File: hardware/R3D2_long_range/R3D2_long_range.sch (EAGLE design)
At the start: 64 parts, among them IC1 ATXMEGA64DA-AU, IC2 NCV8774DT33RKG, IC3 MAX3232CSE, T1 MMBT2222LT1G, T2 ZXMP6A17E6TA, T3 DMN6068SE

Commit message: routing board and remarks taken into account in sch
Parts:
- added C19: 100nF 50V, robotter_capacitor:100NF-E
- added R23, R24: 270-E, robotter_resistor:270-E
- added R25: 10K-F, robotter_resistor:10K-F
- added R26: 150K-F, robotter_resistor:150K-F
- IC1: value ATXMEGA64DA-AU -> ATXMEGA64D4-AU
- PH1: value GP1S58VJ000F -> EESX1106; device robotter_ic:GP1S58VJ000F -> robotter_ic:EESX1106
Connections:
- removed net N$12: IC1.OC0D/PE3, R12.1
- new net LED_COM_3V3: IC1.PC0/OC0A/SDA, R12.1
- new net N$17: IR-SENSOR.2, R23.1
- new net N$18: IR-SENSOR.1, R24.1
- new net VBAT_0-2V: C19.1, IC1.PB2/ADCA10, R25.2, R26.1
- net +24V: now also R26.2
- net GND: now also C19.2, IC1.PB3/ADCA11, R25.1
- net LONG_RANGE_LED_3V3: now also IC1.PA3/ADCA3, R23.2; no longer IC1.PB0/ADCA8/AREF, IR-SENSOR.2
- net LONG_RANGE_SENSOR_OUTPUT_3V3: now also IC1.PC2/OC0C/RXD0; no longer IC1.PC1/OC0B/XCK0/SCL
- net MIRROR_INDEX_3V3: now also IC1.PC3/OC0D/TXD0, IC1.XCK0/OC0B/PD1; no longer IC1.PC5/OC1B/MOSI
- net MOTOR_PWM_3V3: now also IC1.SDA/OC0A/PE0; no longer IC1.OC0A/PD0
- net N$10: now also IC1.OC0D/PE3; no longer IC1.OC0C/PE2
- net N$9: now also IC1.OC0C/PE2; no longer IC1.SCL/OC0B/PE1
- net ON/OFF_SENSOR_3V3: now also IC1.SCL/OC0B/PE1
- net SHORT_RANGE_LED_3V3: now also IC1.PA4/ADCA4, R24.2; no longer IC1.PB1/ADCA9, IR-SENSOR.1
- net SHORT_RANGE_SENSOR_OUTPUT_3V3: now also IC1.PC1/OC0B/XCK0/SCL; no longer IC1.PC2/OC0C/RXD0
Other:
- note added: "BATTERY : 12-30V SUPPLY VOLTAGE"
- note added: "Resistor divider is calculated to output 2V when battery voltage is 31V"
- note added: "Use INTVCC as reference voltage of ADC"
- moved on the sheet: BAT-1, BAT-2, C11, C12, C13, COM, D4, ERROR, IC2, R10, R12, R9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

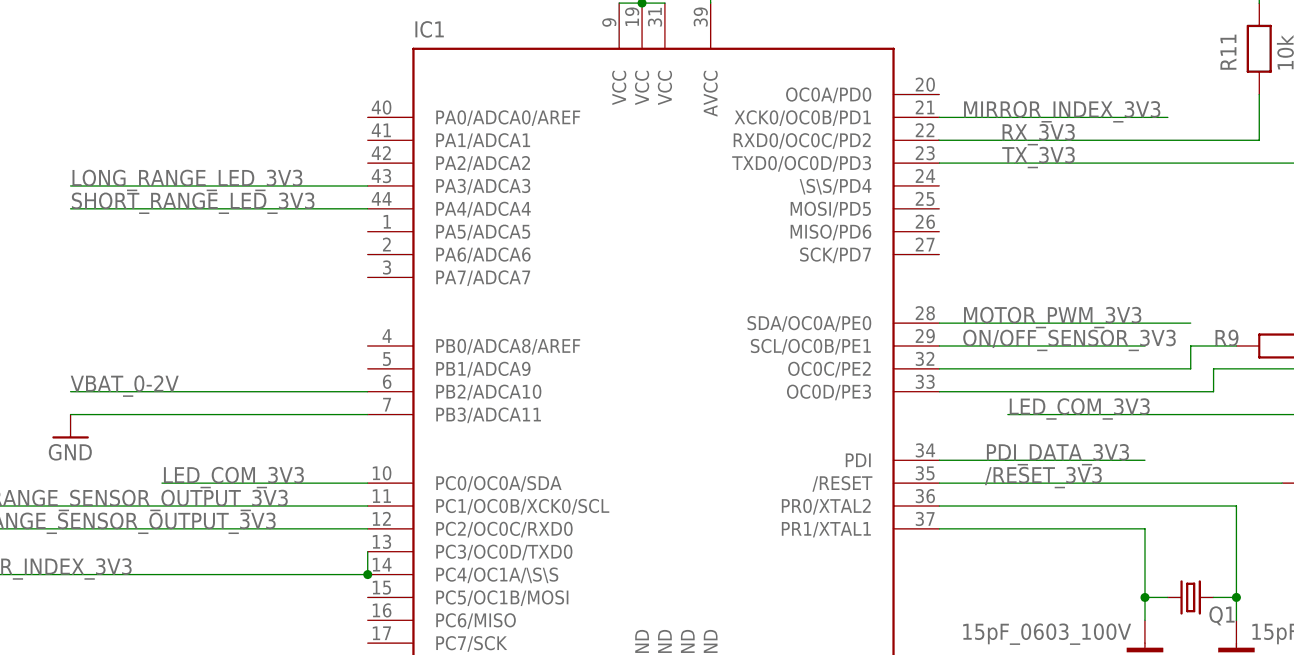
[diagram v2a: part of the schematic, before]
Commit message: com led moved to be viewable with others debug leds
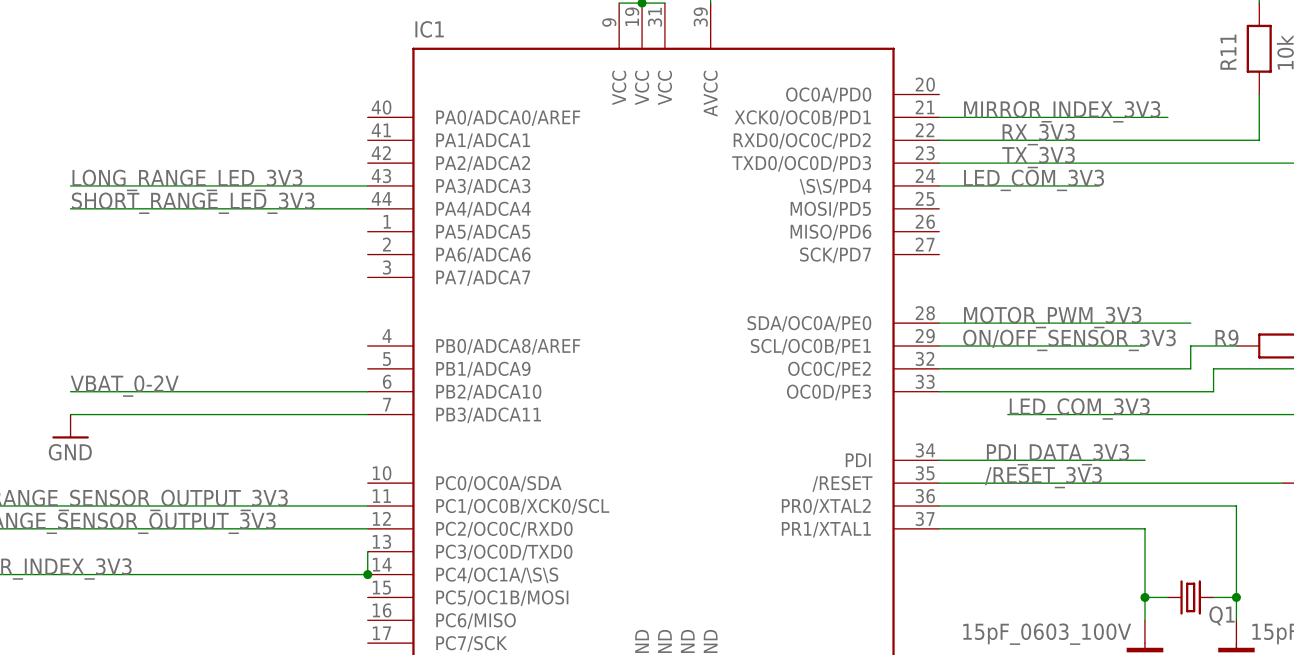
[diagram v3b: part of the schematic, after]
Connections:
- net LED_COM_3V3: now also IC1.\S\S/PD4; no longer IC1.PC0/OC0A/SDA
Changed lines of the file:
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@@
 </segment>
 <segment>
-<pinref part="IC1" gate="G$1" pin="PC0/OC0A/SDA"/>
-<wire x1="76.2" y1="76.2" x2="53.34" y2="76.2" width="0.1524" layer="91"/>
-<label x="53.34" y="76.2" size="1.778" layer="95"/>
+<pinref part="IC1" gate="G$1" pin="\S\S/PD4"/>
+<wire x1="139.7" y1="109.22" x2="157.48" y2="109.22" width="0.1524" layer="91"/>
+<label x="142.24" y="109.22" size="1.778" layer="95"/>
 </segment>
 </net>

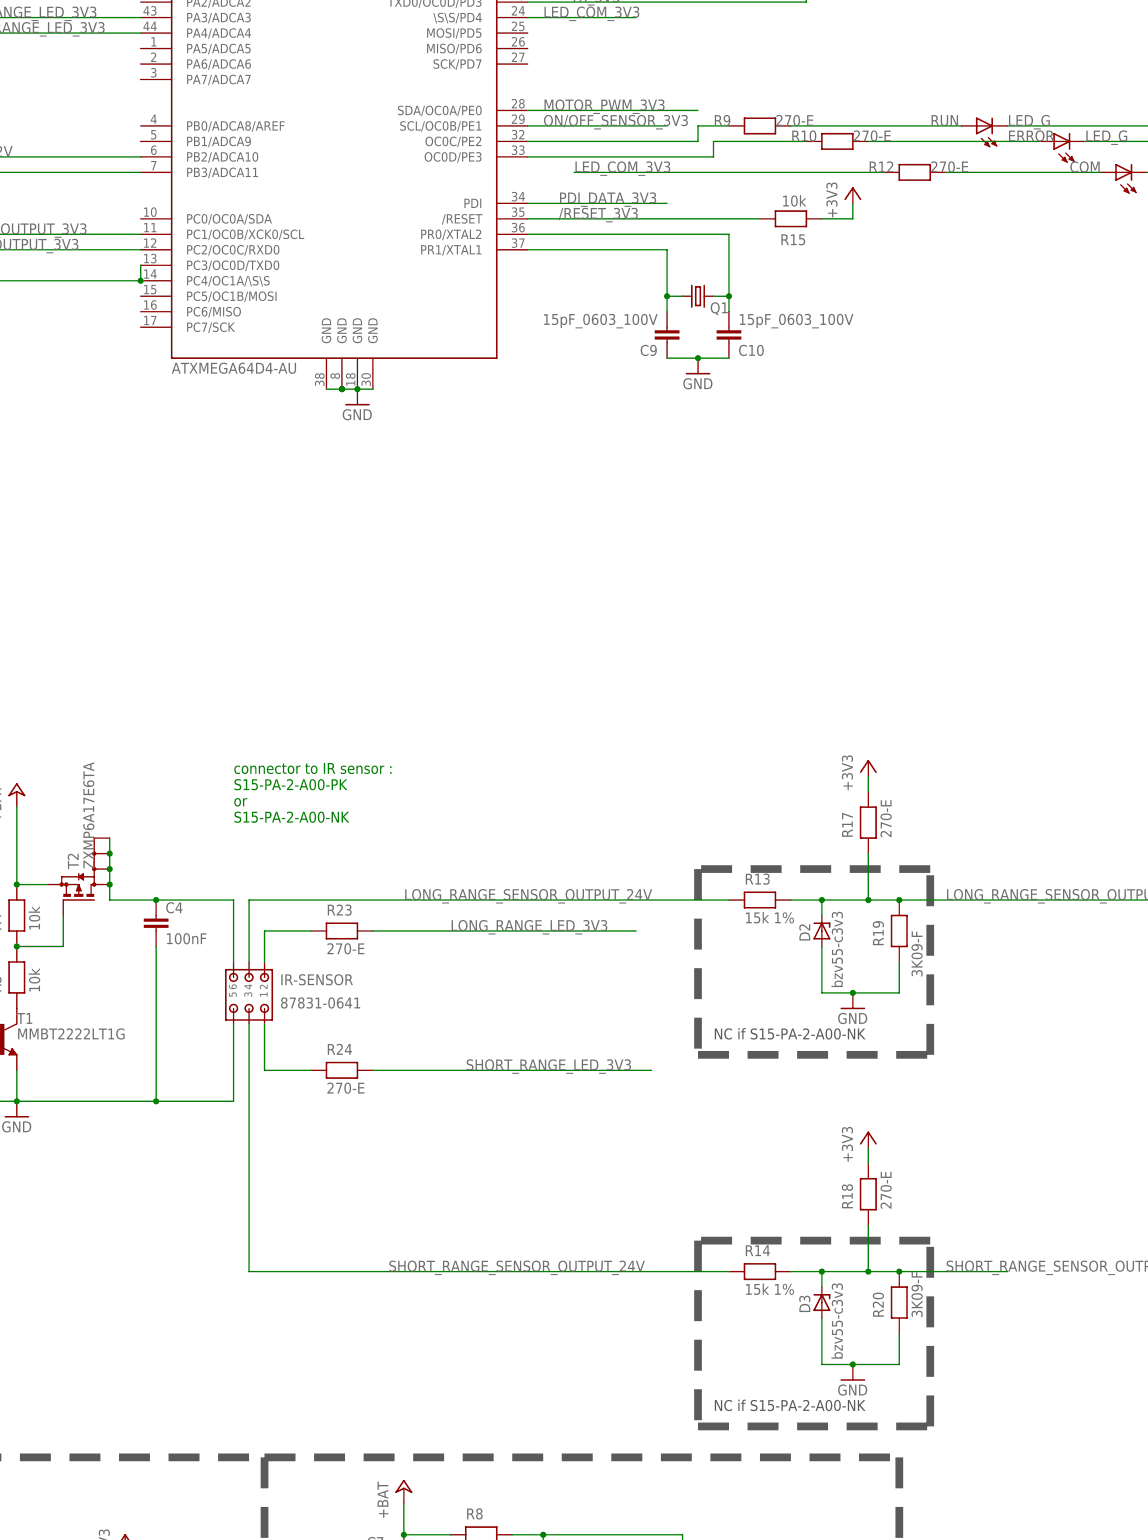
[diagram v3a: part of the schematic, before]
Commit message: R3D2_long_range : some comments added
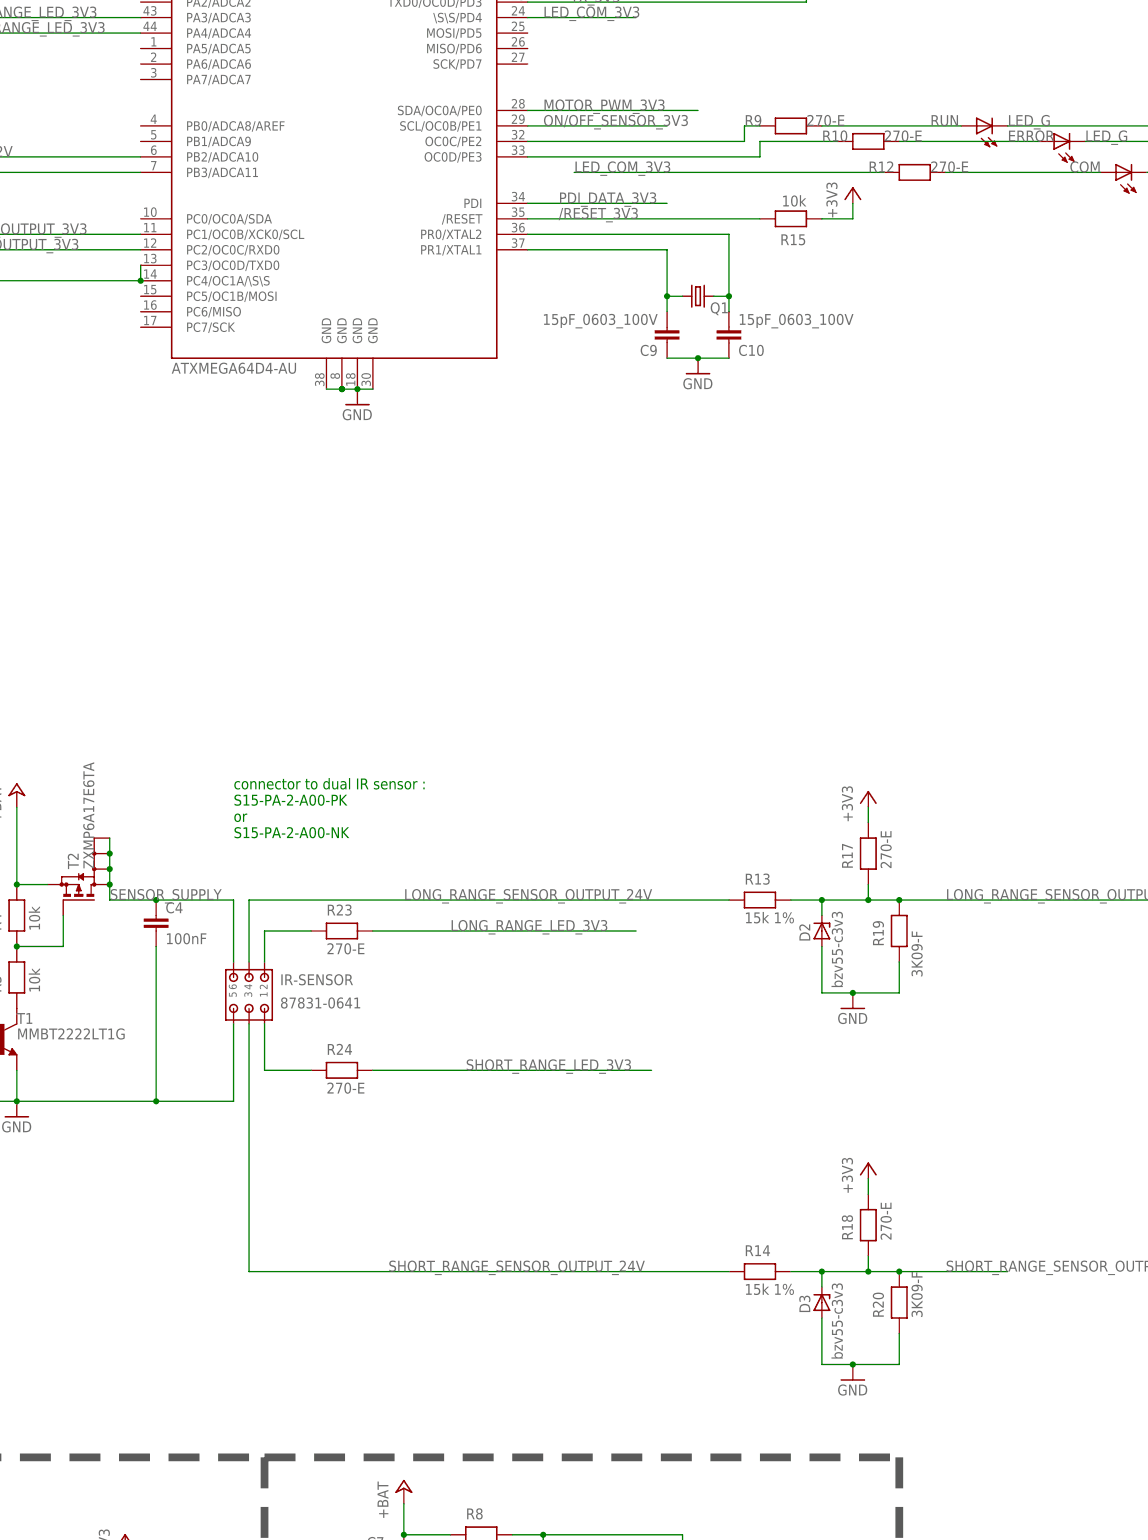
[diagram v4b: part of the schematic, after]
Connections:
- net N$125 renamed SENSOR_SUPPLY
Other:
- note added: "connector to dual IR sensor : S15-PA-2-A00-PK or S15-PA-2-A00-NK"
- note added: "if sensor is S15-PA-2-A00-NK : R13,R14 = 0, D2,D3 = NC, R19,R20 = NC. else if sensor is S15-PA-2-A00-PK : R17,R18 = NC."
- note removed: "NC if S15-PA-2-A00-NK"
- note removed: "connector to IR sensor : S15-PA-2-A00-PK or S15-PA-2-A00-NK"
- moved on the sheet: R10, R17, R18, R9
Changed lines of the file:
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@@
 <?xml version="1.0" encoding="utf-8"?>
 <!DOCTYPE eagle SYSTEM "eagle.dtd">
-<eagle version="6.5.0">
+<eagle version="7.4.0">
 <drawing>
 <settings>
@@
 <wire x1="96.52" y1="-127" x2="96.52" y2="-177.8" width="1.27" layer="97" style="shortdash"/>
 <text x="10.16" y="-132.08" size="1.778" layer="97">sensor head index</text>
-<text x="91.44" y="-22.86" size="1.778" layer="91">connector to IR sensor :
+<text x="91.44" y="-25.4" size="1.778" layer="91">connector to dual IR sensor :
 S15-PA-2-A00-PK
 or
 S15-PA-2-A00-NK</text>
-<wire x1="167.64" y1="-60.96" x2="205.74" y2="-60.96" width="1.27" layer="97" style="shortdash"/>
-<wire x1="205.74" y1="-60.96" x2="205.74" y2="-30.48" width="1.27" layer="97" style="shortdash"/>
-<wire x1="205.74" y1="-30.48" x2="167.64" y2="-30.48" width="1.27" layer="97" style="shortdash"/>
-<wire x1="167.64" y1="-30.48" x2="167.64" y2="-60.96" width="1.27" layer="97" style="shortdash"/>
-<text x="170.18" y="-58.42" size="1.778" layer="97">NC if S15-PA-2-A00-NK</text>
-<wire x1="167.64" y1="-121.92" x2="205.74" y2="-121.92" width="1.27" layer="97" style="shortdash"/>
-<wire x1="205.74" y1="-121.92" x2="205.74" y2="-91.44" width="1.27" layer="97" style="shortdash"/>
-<wire x1="205.74" y1="-91.44" x2="167.64" y2="-91.44" width="1.27" layer="97" style="shortdash"/>
-<wire x1="167.64" y1="-91.44" x2="167.64" y2="-121.92" width="1.27" layer="97" style="shortdash"/>
-<text x="170.18" y="-119.38" size="1.778" layer="97">NC if S15-PA-2-A00-NK</text>
+<wire x1="167.64" y1="-124.46" x2="205.74" y2="-124.46" width="1.27" layer="102" style="shortdash"/>
+<wire x1="205.74" y1="-124.46" x2="205.74" y2="-86.36" width="1.27" layer="102" style="shortdash"/>
+<wire x1="205.74" y1="-86.36" x2="254" y2="-86.36" width="1.27" layer="102" style="shortdash"/>
+<wire x1="254" y1="-86.36" x2="254" y2="-45.72" width="1.27" layer="102" style="shortdash"/>
+<wire x1="254" y1="-45.72" x2="205.74" y2="-45.72" width="1.27" layer="102" style="shortdash"/>
+<wire x1="205.74" y1="-45.72" x2="205.74" y2="-15.24" width="1.27" layer="102" style="shortdash"/>
+<wire x1="205.74" y1="-15.24" x2="167.64" y2="-15.24" width="1.27" layer="102" style="shortdash"/>
+<wire x1="167.64" y1="-15.24" x2="167.64" y2="-124.46" width="1.27" layer="102" style="shortdash"/>
+<text x="198.12" y="-73.66" size="1.778" layer="102">if sensor is S15-PA-2-A00-NK :
+    R13,R14 = 0,
+    D2,D3 = NC,
+    R19,R20 = NC.
+else if sensor is S15-PA-2-A00-PK :
+    R17,R18 = NC.</text>
 <wire x1="96.52" y1="-127" x2="200.66" y2="-127" width="1.27" layer="97" style="shortdash"/>
 <wire x1="200.66" y1="-127" x2="200.66" y2="-157.48" width="1.27" layer="97" style="shortdash"/>
@@
 <instance part="R11" gate="G$1" x="175.26" y="124.46" rot="R90"/>
 <instance part="R16" gate="G$1" x="185.42" y="124.46" rot="R90"/>
-<instance part="R9" gate="G$1" x="177.8" y="91.44" smashed="yes">
-<attribute name="NAME" x="170.18" y="91.44" size="1.778" layer="95"/>
-<attribute name="VALUE" x="180.34" y="91.44" size="1.778" layer="96"/>
-</instance>
-<instance part="R10" gate="G$1" x="190.5" y="88.9" smashed="yes">
-<attribute name="NAME" x="182.88" y="88.9" size="1.778" layer="95"/>
-<attribute name="VALUE" x="193.04" y="88.9" size="1.778" layer="96"/>
+<instance part="R9" gate="G$1" x="182.88" y="91.44" smashed="yes">
+<attribute name="NAME" x="175.26" y="91.44" size="1.778" layer="95"/>
+<attribute name="VALUE" x="185.42" y="91.44" size="1.778" layer="96"/>
+</instance>
+<instance part="R10" gate="G$1" x="195.58" y="88.9" smashed="yes">
+<attribute name="NAME" x="187.96" y="88.9" size="1.778" layer="95"/>
+<attribute name="VALUE" x="198.12" y="88.9" size="1.778" layer="96"/>
 </instance>
 <instance part="R12" gate="G$1" x="203.2" y="83.82" smashed="yes">
@@
 <attribute name="VALUE" x="204.47" y="-48.26" size="1.778" layer="96" rot="R90"/>
 </instance>
-<instance part="R17" gate="G$1" x="195.58" y="-22.86" rot="R90"/>
-<instance part="+3V13" gate="G$1" x="195.58" y="-12.7"/>
+<instance part="R17" gate="G$1" x="195.58" y="-27.94" rot="R90"/>
+<instance part="+3V13" gate="G$1" x="195.58" y="-17.78"/>
 <instance part="R8" gate="G$1" x="132.08" y="-139.7"/>
 <instance part="R13" gate="G$1" x="177.8" y="-35.56"/>
@@
 </instance>
 <instance part="R20" gate="G$1" x="200.66" y="-101.6" rot="R90"/>
-<instance part="R18" gate="G$1" x="195.58" y="-83.82" rot="R90"/>
-<instance part="+3V6" gate="G$1" x="195.58" y="-73.66"/>
+<instance part="R18" gate="G$1" x="195.58" y="-88.9" rot="R90"/>
+<instance part="+3V6" gate="G$1" x="195.58" y="-78.74"/>
 <instance part="R14" gate="G$1" x="177.8" y="-96.52"/>
 <instance part="GND7" gate="1" x="193.04" y="-114.3"/>
@@
 <pinref part="R17" gate="G$1" pin="2"/>
 <pinref part="+3V13" gate="G$1" pin="+3V3"/>
-<wire x1="195.58" y1="-17.78" x2="195.58" y2="-15.24" width="0.1524" layer="91"/>
+<wire x1="195.58" y1="-22.86" x2="195.58" y2="-20.32" width="0.1524" layer="91"/>
 </segment>
 <segment>
 <pinref part="R18" gate="G$1" pin="2"/>
 <pinref part="+3V6" gate="G$1" pin="+3V3"/>
-<wire x1="195.58" y1="-78.74" x2="195.58" y2="-76.2" width="0.1524" layer="91"/>
+<wire x1="195.58" y1="-83.82" x2="195.58" y2="-81.28" width="0.1524" layer="91"/>
 </segment>
 <segment>
@@
 </segment>
 </net>
-<net name="N$125" class="0">
+<net name="SENSOR_SUPPLY" class="0">
 <segment>
 <wire x1="78.74" y1="-35.56" x2="91.44" y2="-35.56" width="0.1524" layer="91"/>
@@
 <junction x="71.12" y="-27.94"/>
 <pinref part="T2" gate="G$1" pin="D@3"/>
+<label x="71.12" y="-35.56" size="1.778" layer="95"/>
 </segment>
 </net>
@@
 <net name="N$2" class="0">
 <segment>
-<wire x1="182.88" y1="91.44" x2="210.82" y2="91.44" width="0.1524" layer="91"/>
+<wire x1="187.96" y1="91.44" x2="210.82" y2="91.44" width="0.1524" layer="91"/>
 <pinref part="R9" gate="G$1" pin="2"/>
 <pinref part="RUN" gate="G$1" pin="A"/>
@@
 <net name="N$4" class="0">
 <segment>
-<wire x1="195.58" y1="88.9" x2="223.52" y2="88.9" width="0.1524" layer="91"/>
+<wire x1="200.66" y1="88.9" x2="223.52" y2="88.9" width="0.1524" layer="91"/>
 <pinref part="R10" gate="G$1" pin="2"/>
 <pinref part="ERROR" gate="G$1" pin="A"/>
@@
 <pinref part="R9" gate="G$1" pin="1"/>
 <pinref part="IC1" gate="G$1" pin="OC0C/PE2"/>
-<wire x1="167.64" y1="91.44" x2="172.72" y2="91.44" width="0.1524" layer="91"/>
-<wire x1="139.7" y1="88.9" x2="167.64" y2="88.9" width="0.1524" layer="91"/>
-<wire x1="167.64" y1="88.9" x2="167.64" y2="91.44" width="0.1524" layer="91"/>
+<wire x1="175.26" y1="91.44" x2="177.8" y2="91.44" width="0.1524" layer="91"/>
+<wire x1="139.7" y1="88.9" x2="175.26" y2="88.9" width="0.1524" layer="91"/>
+<wire x1="175.26" y1="88.9" x2="175.26" y2="91.44" width="0.1524" layer="91"/>
 </segment>
 </net>
@@
 <pinref part="R10" gate="G$1" pin="1"/>
 <pinref part="IC1" gate="G$1" pin="OC0D/PE3"/>
-<wire x1="170.18" y1="88.9" x2="185.42" y2="88.9" width="0.1524" layer="91"/>
-<wire x1="139.7" y1="86.36" x2="170.18" y2="86.36" width="0.1524" layer="91"/>
-<wire x1="170.18" y1="86.36" x2="170.18" y2="88.9" width="0.1524" layer="91"/>
+<wire x1="177.8" y1="88.9" x2="190.5" y2="88.9" width="0.1524" layer="91"/>
+<wire x1="139.7" y1="86.36" x2="177.8" y2="86.36" width="0.1524" layer="91"/>
+<wire x1="177.8" y1="86.36" x2="177.8" y2="88.9" width="0.1524" layer="91"/>
 </segment>
 </net>
@@
 <wire x1="200.66" y1="-35.56" x2="243.84" y2="-35.56" width="0.1524" layer="91"/>
 <wire x1="182.88" y1="-35.56" x2="187.96" y2="-35.56" width="0.1524" layer="91"/>
-<wire x1="195.58" y1="-27.94" x2="195.58" y2="-35.56" width="0.1524" layer="91"/>
+<wire x1="195.58" y1="-33.02" x2="195.58" y2="-35.56" width="0.1524" layer="91"/>
 <wire x1="187.96" y1="-35.56" x2="195.58" y2="-35.56" width="0.1524" layer="91"/>
 <wire x1="195.58" y1="-35.56" x2="200.66" y2="-35.56" width="0.1524" layer="91"/>
@@
 <wire x1="200.66" y1="-96.52" x2="218.44" y2="-96.52" width="0.1524" layer="91"/>
 <wire x1="182.88" y1="-96.52" x2="187.96" y2="-96.52" width="0.1524" layer="91"/>
-<wire x1="195.58" y1="-88.9" x2="195.58" y2="-96.52" width="0.1524" layer="91"/>
+<wire x1="195.58" y1="-93.98" x2="195.58" y2="-96.52" width="0.1524" layer="91"/>
 <wire x1="187.96" y1="-96.52" x2="195.58" y2="-96.52" width="0.1524" layer="91"/>
 <wire x1="195.58" y1="-96.52" x2="200.66" y2="-96.52" width="0.1524" layer="91"/>
